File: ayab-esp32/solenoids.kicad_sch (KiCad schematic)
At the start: 11 parts, among them U301 MCP23017_SS

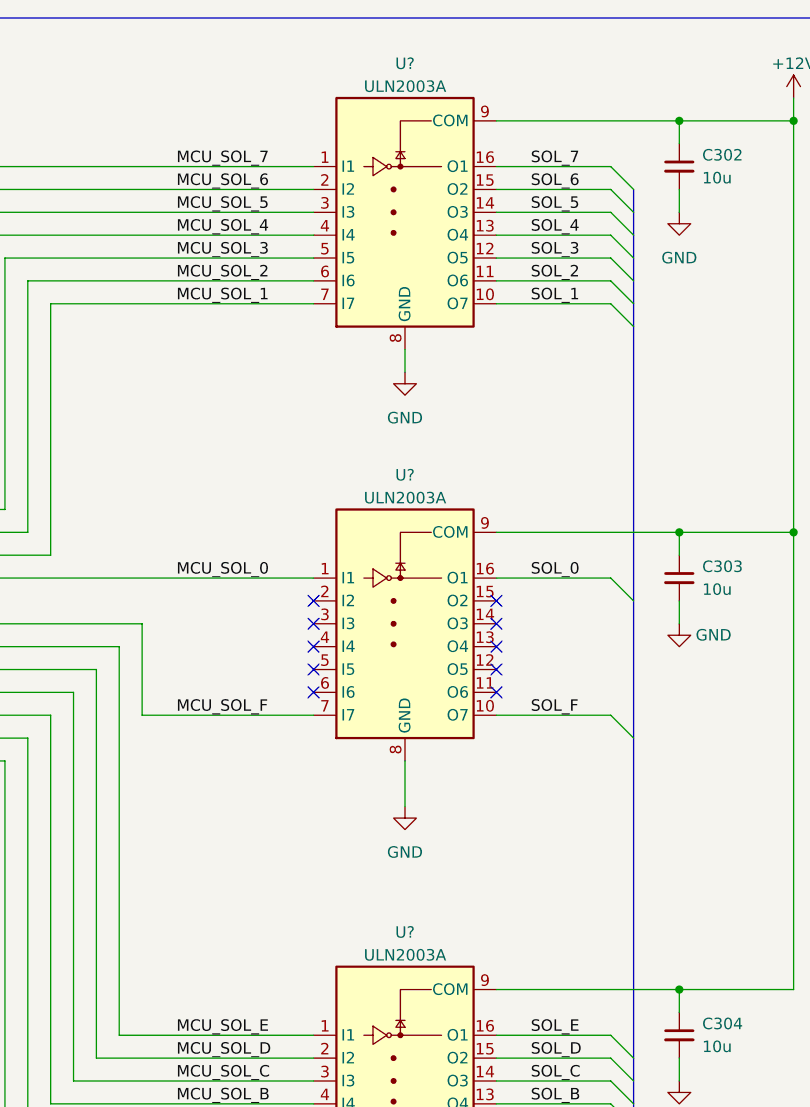
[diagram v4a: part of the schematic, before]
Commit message: clean ERC DRC, fix library paths
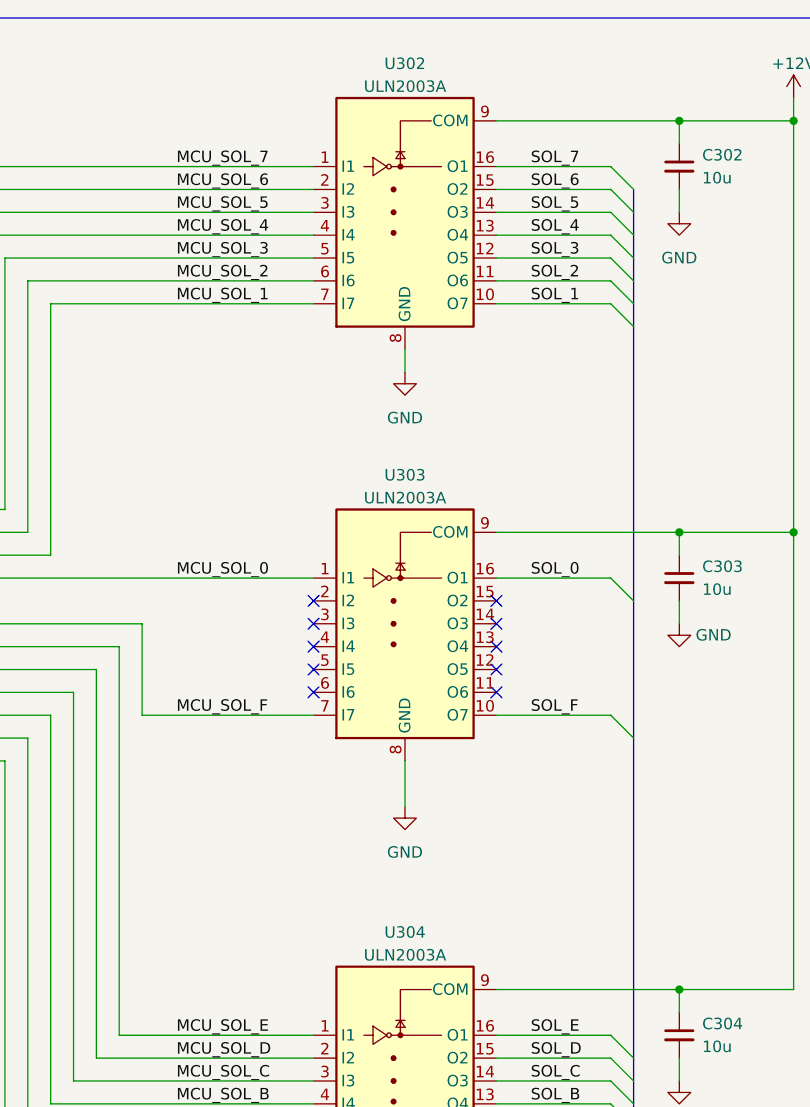
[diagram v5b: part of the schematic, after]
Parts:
- gave numbers to parts that had none: 3
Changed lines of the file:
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@@
 (kicad_sch
-	(version 20231120)
+	(version 20250114)
 	(generator "eeschema")
-	(generator_version "8.0")
+	(generator_version "9.0")
 	(paper "A4")
 	(title_block
@@
 		(comment 2 "distributed under CC-BY-SA-4.0")
 	)
+	(text "unmodified machine is 26W\nassuming all power is \nused by solenoids ~ 130mA each\n\nULN2003A max current 500mA each output\n2.5A package current max\n"
+		(exclude_from_sim no)
+		(at 233.68 93.98 0)
+		(effects
+			(font
+				(size 1.27 1.27)
+			)
+			(justify left bottom)
+		)
+	)
+	(text "SOLENOID DRIVERS"
+		(exclude_from_sim no)
+		(at 20.955 22.86 0)
+		(effects
+			(font
+				(size 1.27 1.27)
+			)
+			(justify left bottom)
+		)
+	)
 	(junction
 		(at 214.63 73.66)
@@
 		)
 	)
-	(text "unmodified machine is 26W\nassuming all power is \nused by solenoids ~ 130mA each\n\nULN2003A max current 500mA each output\n2.5A package current max\n"
-		(exclude_from_sim no)
-		(at 233.68 93.98 0)
-		(effects
-			(font
-				(size 1.27 1.27)
-			)
-			(justify left bottom)
-		)
-	)
-	(text "SOLENOID DRIVERS"
-		(exclude_from_sim no)
-		(at 20.955 22.86 0)
-		(effects
-			(font
-				(size 1.27 1.27)
-			)
-			(justify left bottom)
-		)
-	)
 	(label "MCU_SOL_D"
 		(at 158.75 132.08 0)
-		(fields_autoplaced yes)
 		(effects
 			(font
@@
 	(label "MCU_SOL_C"
 		(at 158.75 134.62 0)
-		(fields_autoplaced yes)
 		(effects
 			(font
@@
 	(label "SOL_F"
 		(at 198.12 93.98 0)
-		(fields_autoplaced yes)
 		(effects
 			(font
@@
 	(label "MCU_SOL_9"
 		(at 158.75 142.24 0)
-		(fields_autoplaced yes)
 		(effects
 			(font
@@
 	(label "SOL_2"
 		(at 198.12 45.72 0)
-		(fields_autoplaced yes)
 		(effects
 			(font
@@
 	(label "MCU_SOL_A"
 		(at 158.75 139.7 0)
-		(fields_autoplaced yes)
 		(effects
 			(font
@@
 	(label "SOL_7"
 		(at 198.12 33.02 0)
-		(fields_autoplaced yes)
 		(effects
 			(font
@@
 	(label "SOL_B"
 		(at 198.12 137.16 0)
-		(fields_autoplaced yes)
 		(effects
 			(font
@@
 	(label "SOL_1"
 		(at 198.12 48.26 0)
-		(fields_autoplaced yes)
 		(effects
 			(font
@@
 	(label "SOL_C"
 		(at 198.12 134.62 0)
-		(fields_autoplaced yes)
 		(effects
 			(font
@@
 	(label "MCU_SOL_2"
 		(at 158.75 45.72 0)
-		(fields_autoplaced yes)
 		(effects
 			(font
@@
 	(label "MCU_SOL_8"
 		(at 158.75 144.78 0)
-		(fields_autoplaced yes)
 		(effects
 			(font
@@
 	(label "SOL_5"
 		(at 198.12 38.1 0)
-		(fields_autoplaced yes)
 		(effects
 			(font
@@
 	(label "SOL_E"
 		(at 198.12 129.54 0)
-		(fields_autoplaced yes)
 		(effects
 			(font
@@
 	(label "SOL_8"
 		(at 198.12 144.78 0)
-		(fields_autoplaced yes)
 		(effects
 			(font
@@
 	(label "MCU_SOL_B"
 		(at 158.75 137.16 0)
-		(fields_autoplaced yes)
 		(effects
 			(font
@@
 	(label "MCU_SOL_7"
 		(at 158.75 33.02 0)
-		(fields_autoplaced yes)
 		(effects
 			(font
@@
 	(label "SOL_9"
 		(at 198.12 142.24 0)
-		(fields_autoplaced yes)
 		(effects
 			(font
@@
 	(label "SOL_0"
 		(at 198.12 78.74 0)
-		(fields_autoplaced yes)
 		(effects
 			(font
@@
 	(label "MCU_SOL_F"
 		(at 158.75 93.98 0)
-		(fields_autoplaced yes)
 		(effects
 			(font
@@
 	(label "MCU_SOL_E"
 		(at 158.75 129.54 0)
-		(fields_autoplaced yes)
 		(effects
 			(font
@@
 	(label "MCU_SOL_3"
 		(at 158.75 43.18 0)
-		(fields_autoplaced yes)
 		(effects
 			(font
@@
 	(label "SOL_A"
 		(at 198.12 139.7 0)
-		(fields_autoplaced yes)
 		(effects
 			(font
@@
 	(label "MCU_SOL_6"
 		(at 158.75 35.56 0)
-		(fields_autoplaced yes)
 		(effects
 			(font
@@
 	(label "SOL_3"
 		(at 198.12 43.18 0)
-		(fields_autoplaced yes)
 		(effects
 			(font
@@
 	(label "MCU_SOL_1"
 		(at 158.75 48.26 0)
-		(fields_autoplaced yes)
 		(effects
 			(font
@@
 	(label "MCU_SOL_0"
 		(at 158.75 78.74 0)
-		(fields_autoplaced yes)
 		(effects
 			(font
@@
 	(label "MCU_SOL_5"
 		(at 158.75 38.1 0)
-		(fields_autoplaced yes)
 		(effects
 			(font
@@
 	(label "SOL_6"
 		(at 198.12 35.56 0)
-		(fields_autoplaced yes)
 		(effects
 			(font
@@
 	(label "MCU_SOL_4"
 		(at 158.75 40.64 0)
-		(fields_autoplaced yes)
 		(effects
 			(font
@@
 	(label "SOL_D"
 		(at 198.12 132.08 0)
-		(fields_autoplaced yes)
 		(effects
 			(font
@@
 	(label "SOL_4"
 		(at 198.12 40.64 0)
-		(fields_autoplaced yes)
 		(effects
 			(font
@@
 		(shape bidirectional)
 		(at 66.04 69.85 180)
-		(fields_autoplaced yes)
 		(effects
 			(font
@@
 		(shape input)
 		(at 66.04 72.39 180)
-		(fields_autoplaced yes)
 		(effects
 			(font
@@
 		(shape output)
 		(at 212.09 152.4 0)
-		(fields_autoplaced yes)
 		(effects
 			(font
@@
 		(dnp no)
 		(fields_autoplaced yes)
-		(property "Reference" "#PWR0104"
+		(property "Reference" "#PWR0306"
 			(at 184.15 158.75 0)
 			(effects
@@
 			)
 		)
-		(property "Description" ""
+		(property "Description" "Power symbol creates a global label with name \"GND\" , ground"
 			(at 184.15 152.4 0)
 			(effects
@@
 		(dnp no)
 		(fields_autoplaced yes)
-		(property "Reference" "U?"
+		(property "Reference" "U302"
 			(at 184.15 21.59 0)
 			(effects
@@
 			)
 		)
-		(property "Description" ""
+		(property "Description" "Power symbol creates a global label with name \"+3V3\""
 			(at 97.79 48.26 0)
 			(effects
@@
 		(dnp no)
 		(fields_autoplaced yes)
-		(property "Reference" "#PWR0101"
+		(property "Reference" "#PWR0305"
 			(at 184.15 110.49 0)
 			(effects
@@
 			)
 		)
-		(property "Description" ""
+		(property "Description" "Power symbol creates a global label with name \"GND\" , ground"
 			(at 184.15 104.14 0)
 			(effects
@@
 		(dnp no)
 		(fields_autoplaced yes)
-		(property "Reference" "U?"
+		(property "Reference" "U303"
 			(at 184.15 67.31 0)
 			(effects
@@
 		(on_board yes)
 		(dnp no)
-		(property "Reference" "#PWR0104"
+		(property "Reference" "#PWR0301"
 			(at 59.69 66.04 0)
 			(effects
@@
 			)
 		)
-		(property "Description" ""
+		(property "Description" "Power symbol creates a global label with name \"GND\" , ground"
 			(at 59.69 59.69 0)
 			(effects
@@
 		(on_board yes)
 		(dnp no)
-		(property "Reference" "#PWR0104"
+		(property "Reference" "#PWR0308"
 			(at 214.63 90.17 0)
 			(effects
@@
 			)
 		)
-		(property "Description" ""
+		(property "Description" "Power symbol creates a global label with name \"GND\" , ground"
 			(at 214.63 83.82 0)
 			(effects
@@
 		(dnp no)
 		(fields_autoplaced yes)
-		(property "Reference" "#PWR0102"
+		(property "Reference" "#PWR0304"
 			(at 184.15 62.23 0)
 			(effects
@@
 			)
 		)
-		(property "Description" ""
+		(property "Description" "Power symbol creates a global label with name \"GND\" , ground"
 			(at 184.15 55.88 0)
 			(effects
@@
 		(dnp no)
 		(fields_autoplaced yes)
-		(property "Reference" "#PWR0101"
+		(property "Reference" "#PWR0303"
 			(at 97.79 120.65 0)
 			(effects
@@
 			)
 		)
-		(property "Description" ""
+		(property "Description" "Power symbol creates a global label with name \"GND\" , ground"
 			(at 97.79 114.3 0)
 			(effects
@@
 		(dnp no)
 		(fields_autoplaced yes)
-		(property "Reference" "#PWR0104"
+		(property "Reference" "#PWR0307"
 			(at 214.63 44.45 0)
 			(effects
@@
 			)
 		)
-		(property "Description" ""
+		(property "Description" "Power symbol creates a global label with name \"GND\" , ground"
 			(at 214.63 38.1 0)
 			(effects
@@
 		(dnp no)
 		(fields_autoplaced yes)
-		(property "Reference" "U?"
+		(property "Reference" "U304"
 			(at 184.15 118.11 0)
 			(effects
@@
 		(dnp no)
 		(fields_autoplaced yes)
-		(property "Reference" "#PWR0106"
+		(property "Reference" "#PWR0310"
 			(at 227.33 29.21 0)
 			(effects
@@
 			)
 		)
-		(property "Description" ""
+		(property "Description" "Power symbol creates a global label with name \"+12V\""
 			(at 227.33 25.4 0)
 			(effects
@@
 		(dnp no)
 		(fields_autoplaced yes)
-		(property "Reference" "#PWR0104"
+		(property "Reference" "#PWR0309"
 			(at 214.63 140.97 0)
 			(effects
@@
 			)
 		)
-		(property "Description" ""
+		(property "Description" "Power symbol creates a global label with name \"GND\" , ground"
 			(at 214.63 134.62 0)
 			(effects
